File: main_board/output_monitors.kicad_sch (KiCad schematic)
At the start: 52 parts, among them U14 TL072CDR, U17 TL072CDR, U18 TL072CDR, U4 TL072CDR

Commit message: Upgrades board to v5. Adds Bonk Daddy.
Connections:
- net GND: now also R100.1, R69.1, R70.1, R71.1, R72.1, R97.1, R98.1, R99.1; no longer U14.3 (+), U14.5 (+), U17.3 (+), U17.5 (+), U18.3 (+), U18.5 (+), U4.3 (+), U4.5 (+)
- net Out0: now also U4.3 (+); no longer R69.1
- net Out1: now also U4.5 (+); no longer R70.1
- net Out2: now also U14.3 (+); no longer R71.1
- net Out3: now also U14.5 (+); no longer R72.1
- net Out4: now also U17.3 (+); no longer R97.1
- net Out5: now also U17.5 (+); no longer R98.1
- net Out6: now also U18.3 (+); no longer R99.1
- net Out7: now also U18.5 (+); no longer R100.1
- net at R72.2, U14.6 (-): now also D24.2 (A), D28.1 (K); no longer D24.1 (K), D28.2 (A)
- net at R100.2, U18.6 (-): now also D32.2 (A), D36.1 (K); no longer D32.1 (K), D36.2 (A)
- net at D29.2 (A), D33.1 (K): now also R97.2, U17.2 (-); no longer U17.1
- net at D29.1 (K), D33.2 (A): now also U17.1; no longer R97.2, U17.2 (-)
- net at R69.2, U4.2 (-): now also D21.2 (A), D25.1 (K); no longer D21.1 (K), D25.2 (A)
- net at D23.2 (A), D27.1 (K): now also R71.2, U14.2 (-); no longer U14.1
- net at D23.1 (K), D27.2 (A): now also U14.1; no longer R71.2, U14.2 (-)
- net at D31.1 (K), D35.2 (A): now also U18.1; no longer R99.2, U18.2 (-)
- net at D31.2 (A), D35.1 (K): now also R99.2, U18.2 (-); no longer U18.1
- net at D30.2 (A), D34.1 (K): now also R98.2, U17.6 (-); no longer U17.7
- net at D30.1 (K), D34.2 (A): now also U17.7; no longer R98.2, U17.6 (-)
- net at D22.2 (A), D26.1 (K): now also R70.2, U4.6 (-); no longer U4.7
- net at D22.1 (K), D26.2 (A): now also U4.7; no longer R70.2, U4.6 (-)
- new net: D24.1 (K), D28.2 (A), U14.7
- new net: D32.1 (K), D36.2 (A), U18.7
- new net: D21.1 (K), D25.2 (A), U4.1
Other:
- moved on the sheet: D21, D22, D23, D24, D25, D26, D27, D28, D29, D30, D31, D32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

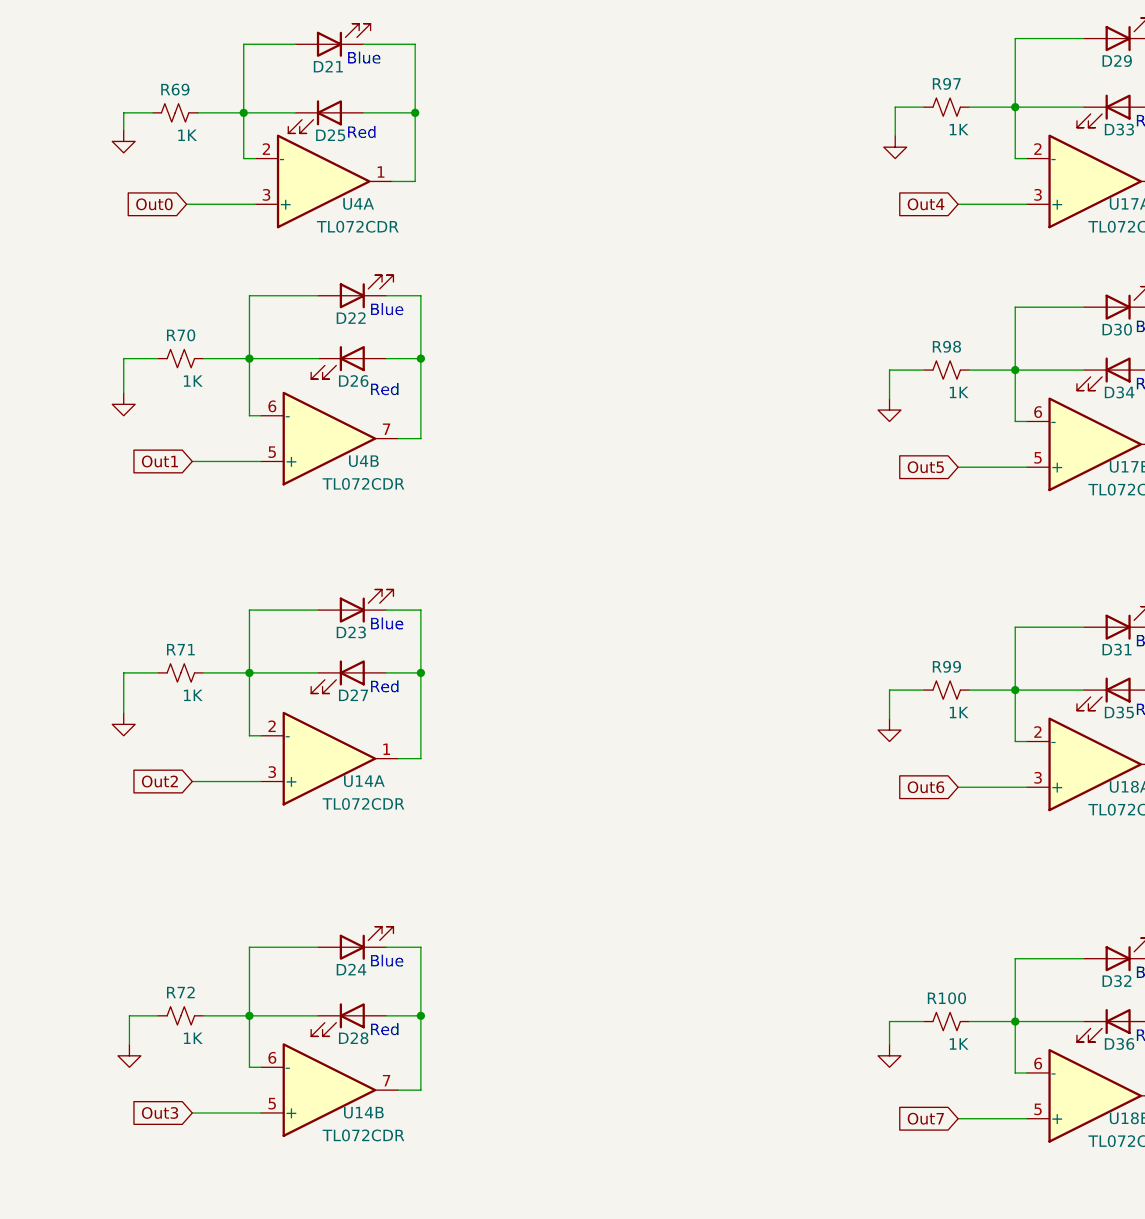
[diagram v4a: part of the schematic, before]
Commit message: LED current resistors now 2,.2K
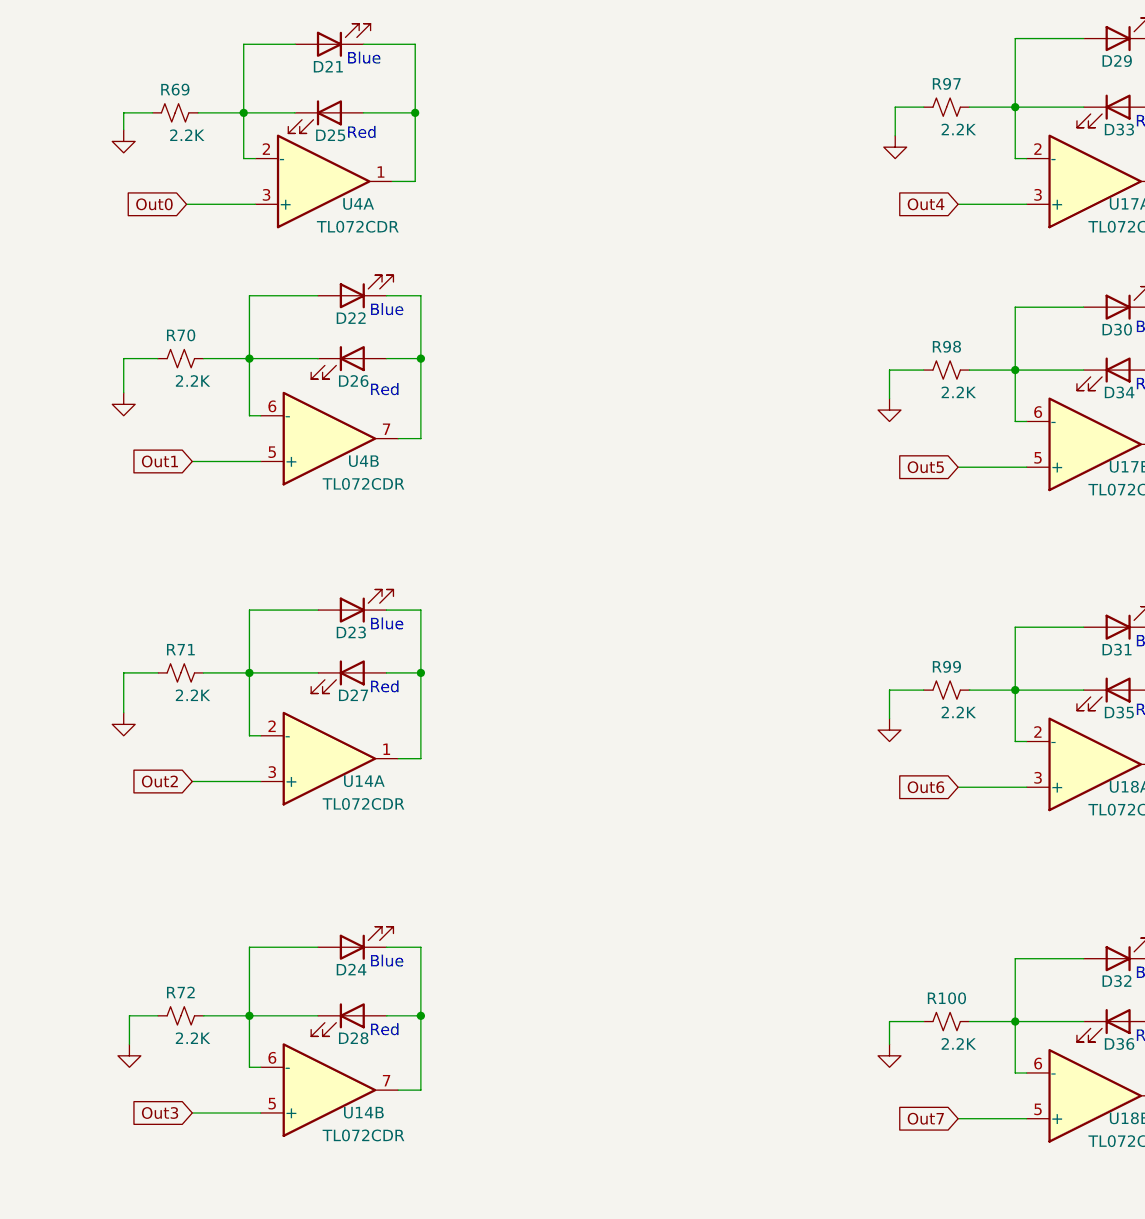
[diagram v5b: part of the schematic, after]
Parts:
- R100, R69, R70, R71, R72, R97, R98, R99: value 1K -> 2.2K;  LCSC Part # C17513 -> C17520
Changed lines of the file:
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@@
     (in_bom yes) (on_board yes)
     (property "Reference" "R72" (id 0) (at 79.375 125.095 90))
-    (property "Value" "1K" (id 1) (at 80.645 130.175 90))
+    (property "Value" "2.2K" (id 1) (at 80.645 130.175 90))
     (property "Footprint" "Resistor_SMD:R_0805_2012Metric_Pad1.20x1.40mm_HandSolder" (id 2) (at 79.375 127.635 0)
       (effects (font (size 1.27 1.27)) hide)
@@
       (effects (font (size 1.27 1.27)) hide)
     )
-    (property " LCSC Part #" "C17513" (id 5) (at 79.375 127.635 0)
+    (property " LCSC Part #" "C17520" (id 5) (at 79.375 127.635 0)
       (effects (font (size 1.27 1.27)) hide)
     )
@@
     (in_bom yes) (on_board yes)
     (property "Reference" "R100" (id 0) (at 164.465 125.73 90))
-    (property "Value" "1K" (id 1) (at 165.735 130.81 90))
+    (property "Value" "2.2K" (id 1) (at 165.735 130.81 90))
     (property "Footprint" "Resistor_SMD:R_0805_2012Metric_Pad1.20x1.40mm_HandSolder" (id 2) (at 164.465 128.27 0)
       (effects (font (size 1.27 1.27)) hide)
@@
       (effects (font (size 1.27 1.27)) hide)
     )
-    (property " LCSC Part #" "C17513" (id 5) (at 164.465 128.27 0)
+    (property " LCSC Part #" "C17520" (id 5) (at 164.465 128.27 0)
       (effects (font (size 1.27 1.27)) hide)
     )
@@
     (in_bom yes) (on_board yes)
     (property "Reference" "R69" (id 0) (at 78.74 24.765 90))
-    (property "Value" "1K" (id 1) (at 80.01 29.845 90))
+    (property "Value" "2.2K" (id 1) (at 80.01 29.845 90))
     (property "Footprint" "Resistor_SMD:R_0805_2012Metric_Pad1.20x1.40mm_HandSolder" (id 2) (at 78.74 27.305 0)
       (effects (font (size 1.27 1.27)) hide)
@@
       (effects (font (size 1.27 1.27)) hide)
     )
-    (property " LCSC Part #" "C17513" (id 5) (at 78.74 27.305 0)
+    (property " LCSC Part #" "C17520" (id 5) (at 78.74 27.305 0)
       (effects (font (size 1.27 1.27)) hide)
     )
@@
     (in_bom yes) (on_board yes)
     (property "Reference" "R99" (id 0) (at 164.465 88.9 90))
-    (property "Value" "1K" (id 1) (at 165.735 93.98 90))
+    (property "Value" "2.2K" (id 1) (at 165.735 93.98 90))
     (property "Footprint" "Resistor_SMD:R_0805_2012Metric_Pad1.20x1.40mm_HandSolder" (id 2) (at 164.465 91.44 0)
       (effects (font (size 1.27 1.27)) hide)
@@
       (effects (font (size 1.27 1.27)) hide)
     )
-    (property " LCSC Part #" "C17513" (id 5) (at 164.465 91.44 0)
+    (property " LCSC Part #" "C17520" (id 5) (at 164.465 91.44 0)
       (effects (font (size 1.27 1.27)) hide)
     )
@@
     (in_bom yes) (on_board yes)
     (property "Reference" "R98" (id 0) (at 164.465 53.34 90))
-    (property "Value" "1K" (id 1) (at 165.735 58.42 90))
+    (property "Value" "2.2K" (id 1) (at 165.735 58.42 90))
     (property "Footprint" "Resistor_SMD:R_0805_2012Metric_Pad1.20x1.40mm_HandSolder" (id 2) (at 164.465 55.88 0)
       (effects (font (size 1.27 1.27)) hide)
@@
       (effects (font (size 1.27 1.27)) hide)
     )
-    (property " LCSC Part #" "C17513" (id 5) (at 164.465 55.88 0)
+    (property " LCSC Part #" "C17520" (id 5) (at 164.465 55.88 0)
       (effects (font (size 1.27 1.27)) hide)
     )
@@
     (in_bom yes) (on_board yes)
     (property "Reference" "R70" (id 0) (at 79.375 52.07 90))
-    (property "Value" "1K" (id 1) (at 80.645 57.15 90))
+    (property "Value" "2.2K" (id 1) (at 80.645 57.15 90))
     (property "Footprint" "Resistor_SMD:R_0805_2012Metric_Pad1.20x1.40mm_HandSolder" (id 2) (at 79.375 54.61 0)
       (effects (font (size 1.27 1.27)) hide)
@@
       (effects (font (size 1.27 1.27)) hide)
     )
-    (property " LCSC Part #" "C17513" (id 5) (at 79.375 54.61 0)
+    (property " LCSC Part #" "C17520" (id 5) (at 79.375 54.61 0)
       (effects (font (size 1.27 1.27)) hide)
     )
@@
     (in_bom yes) (on_board yes)
     (property "Reference" "R71" (id 0) (at 79.375 86.995 90))
-    (property "Value" "1K" (id 1) (at 80.645 92.075 90))
+    (property "Value" "2.2K" (id 1) (at 80.645 92.075 90))
     (property "Footprint" "Resistor_SMD:R_0805_2012Metric_Pad1.20x1.40mm_HandSolder" (id 2) (at 79.375 89.535 0)
       (effects (font (size 1.27 1.27)) hide)
@@
       (effects (font (size 1.27 1.27)) hide)
     )
-    (property " LCSC Part #" "C17513" (id 5) (at 79.375 89.535 0)
+    (property " LCSC Part #" "C17520" (id 5) (at 79.375 89.535 0)
       (effects (font (size 1.27 1.27)) hide)
     )
@@
     (in_bom yes) (on_board yes)
     (property "Reference" "R97" (id 0) (at 164.465 24.13 90))
-    (property "Value" "1K" (id 1) (at 165.735 29.21 90))
+    (property "Value" "2.2K" (id 1) (at 165.735 29.21 90))
     (property "Footprint" "Resistor_SMD:R_0805_2012Metric_Pad1.20x1.40mm_HandSolder" (id 2) (at 164.465 26.67 0)
       (effects (font (size 1.27 1.27)) hide)
@@
       (effects (font (size 1.27 1.27)) hide)
     )
-    (property " LCSC Part #" "C17513" (id 5) (at 164.465 26.67 0)
-      (effects (font (size 1.27 1.27)) hide)
-    )
+    (property " LCSC Part #" "C17520" (id 5) (at 164.465 26.67 0)
+      (effects (font (size 1.27 1.27)) hide)
+    )

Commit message: Updates main_board, uses generate_boms.bat
Updates reverse protection circuitry on main board.
Updates 3.3V reference circuitry.
Uses generate_boms and retires .xlsx BOM files.
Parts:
- C35, C36, C37, C38, C39, C40, C41, C42:  LCSC Part # C49678 -> (none); LCSC Part # (none) -> C49678
- R100, R69, R70, R71, R72, R97, R98, R99:  LCSC Part # C17520 -> (none); LCSC Part # (none) -> C17520
- U14, U17, U18, U4:  LCSC Part # C6961 -> (none); LCSC Part # (none) -> C6961
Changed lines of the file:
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@@
       (effects (font (size 1.27 1.27)) hide)
     )
-    (property " LCSC Part #" "C6961" (id 5) (at 57.15 172.72 0)
+    (property "LCSC Part #" "C6961" (id 5) (at 57.15 172.72 0)
       (effects (font (size 1.27 1.27)) hide)
     )
@@
       (effects (font (size 1.27 1.27)) hide)
     )
-    (property " LCSC Part #" "C17520" (id 5) (at 79.375 127.635 0)
+    (property "LCSC Part #" "C17520" (id 5) (at 79.375 127.635 0)
       (effects (font (size 1.27 1.27)) hide)
     )
@@
       (effects (font (size 1.27 1.27)) hide)
     )
-    (property " LCSC Part #" "C6961" (id 5) (at 180.975 136.525 0)
+    (property "LCSC Part #" "C6961" (id 5) (at 180.975 136.525 0)
       (effects (font (size 1.27 1.27)) hide)
     )
@@
       (effects (font (size 1.27 1.27)) hide)
     )
-    (property " LCSC Part #" "C6961" (id 5) (at 180.975 34.925 0)
+    (property "LCSC Part #" "C6961" (id 5) (at 180.975 34.925 0)
       (effects (font (size 1.27 1.27)) hide)
     )
@@
       (effects (font (size 1.27 1.27)) hide)
     )
-    (property " LCSC Part #" "C17520" (id 5) (at 164.465 128.27 0)
+    (property "LCSC Part #" "C17520" (id 5) (at 164.465 128.27 0)
       (effects (font (size 1.27 1.27)) hide)
     )
@@
       (effects (font (size 1.27 1.27)) hide)
     )
-    (property " LCSC Part #" "C17520" (id 5) (at 78.74 27.305 0)
+    (property "LCSC Part #" "C17520" (id 5) (at 78.74 27.305 0)
       (effects (font (size 1.27 1.27)) hide)
     )
@@
       (effects (font (size 1.27 1.27)) hide)
     )
-    (property " LCSC Part #" "C17520" (id 5) (at 164.465 91.44 0)
+    (property "LCSC Part #" "C17520" (id 5) (at 164.465 91.44 0)
       (effects (font (size 1.27 1.27)) hide)
     )
@@
       (effects (font (size 1.27 1.27)) hide)
     )
-    (property " LCSC Part #" "C49678" (id 5) (at 150.495 179.705 0)
+    (property "LCSC Part #" "C49678" (id 5) (at 150.495 179.705 0)
       (effects (font (size 1.27 1.27)) hide)
     )
@@
       (effects (font (size 1.27 1.27)) hide)
     )
-    (property " LCSC Part #" "C17520" (id 5) (at 164.465 55.88 0)
+    (property "LCSC Part #" "C17520" (id 5) (at 164.465 55.88 0)
       (effects (font (size 1.27 1.27)) hide)
     )
@@
       (effects (font (size 1.27 1.27)) hide)
     )
-    (property " LCSC Part #" "C17520" (id 5) (at 79.375 54.61 0)
+    (property "LCSC Part #" "C17520" (id 5) (at 79.375 54.61 0)
       (effects (font (size 1.27 1.27)) hide)
     )
@@
       (effects (font (size 1.27 1.27)) hide)
     )
-    (property " LCSC Part #" "C6961" (id 5) (at 36.83 172.72 0)
+    (property "LCSC Part #" "C6961" (id 5) (at 36.83 172.72 0)
       (effects (font (size 1.27 1.27)) hide)
     )
@@
       (effects (font (size 1.27 1.27)) hide)
     )
-    (property " LCSC Part #" "C6961" (id 5) (at 95.885 63.5 0)
+    (property "LCSC Part #" "C6961" (id 5) (at 95.885 63.5 0)
       (effects (font (size 1.27 1.27)) hide)
     )
@@
       (effects (font (size 1.27 1.27)) hide)
     )
-    (property " LCSC Part #" "C6961" (id 5) (at 180.975 99.695 0)
+    (property "LCSC Part #" "C6961" (id 5) (at 180.975 99.695 0)
       (effects (font (size 1.27 1.27)) hide)
     )
@@
       (effects (font (size 1.27 1.27)) hide)
     )
-    (property " LCSC Part #" "C17520" (id 5) (at 79.375 89.535 0)
+    (property "LCSC Part #" "C17520" (id 5) (at 79.375 89.535 0)
       (effects (font (size 1.27 1.27)) hide)
     )
@@
       (effects (font (size 1.27 1.27)) hide)
     )
-    (property " LCSC Part #" "C6961" (id 5) (at 95.885 99.06 0)
+    (property "LCSC Part #" "C6961" (id 5) (at 95.885 99.06 0)
       (effects (font (size 1.27 1.27)) hide)
     )
@@
       (effects (font (size 1.27 1.27)) hide)
     )
-    (property " LCSC Part #" "C49678" (id 5) (at 142.875 179.705 0)
+    (property "LCSC Part #" "C49678" (id 5) (at 142.875 179.705 0)
       (effects (font (size 1.27 1.27)) hide)
     )
@@
       (effects (font (size 1.27 1.27)) hide)
     )
-    (property " LCSC Part #" "C6961" (id 5) (at 46.99 172.72 0)
+    (property "LCSC Part #" "C6961" (id 5) (at 46.99 172.72 0)
       (effects (font (size 1.27 1.27)) hide)
     )
@@
       (effects (font (size 1.27 1.27)) hide)
     )
-    (property " LCSC Part #" "C17520" (id 5) (at 164.465 26.67 0)
+    (property "LCSC Part #" "C17520" (id 5) (at 164.465 26.67 0)
       (effects (font (size 1.27 1.27)) hide)
     )
@@
       (effects (font (size 1.27 1.27)) hide)
     )
-    (property " LCSC Part #" "C49678" (id 5) (at 135.255 168.275 0)
+    (property "LCSC Part #" "C49678" (id 5) (at 135.255 168.275 0)
       (effects (font (size 1.27 1.27)) hide)
     )
@@
       (effects (font (size 1.27 1.27)) hide)
     )
-    (property " LCSC Part #" "C49678" (id 5) (at 135.255 179.705 0)
+    (property "LCSC Part #" "C49678" (id 5) (at 135.255 179.705 0)
       (effects (font (size 1.27 1.27)) hide)
     )
@@
       (effects (font (size 1.27 1.27)) hide)
     )
-    (property " LCSC Part #" "C49678" (id 5) (at 150.495 168.275 0)
+    (property "LCSC Part #" "C49678" (id 5) (at 150.495 168.275 0)
       (effects (font (size 1.27 1.27)) hide)
     )
@@
       (effects (font (size 1.27 1.27)) hide)
     )
-    (property " LCSC Part #" "C49678" (id 5) (at 127.635 168.275 0)
+    (property "LCSC Part #" "C49678" (id 5) (at 127.635 168.275 0)
       (effects (font (size 1.27 1.27)) hide)
     )
@@
       (effects (font (size 1.27 1.27)) hide)
     )
-    (property " LCSC Part #" "C6961" (id 5) (at 95.25 34.925 0)
+    (property "LCSC Part #" "C6961" (id 5) (at 95.25 34.925 0)
       (effects (font (size 1.27 1.27)) hide)
     )
@@
       (effects (font (size 1.27 1.27)) hide)
     )
-    (property " LCSC Part #" "C49678" (id 5) (at 142.875 168.275 0)
+    (property "LCSC Part #" "C49678" (id 5) (at 142.875 168.275 0)
       (effects (font (size 1.27 1.27)) hide)
     )
@@
       (effects (font (size 1.27 1.27)) hide)
     )
-    (property " LCSC Part #" "C6961" (id 5) (at 180.975 64.135 0)
+    (property "LCSC Part #" "C6961" (id 5) (at 180.975 64.135 0)
       (effects (font (size 1.27 1.27)) hide)
     )
@@
       (effects (font (size 1.27 1.27)) hide)
     )
-    (property " LCSC Part #" "C49678" (id 5) (at 127.635 179.705 0)
+    (property "LCSC Part #" "C49678" (id 5) (at 127.635 179.705 0)
       (effects (font (size 1.27 1.27)) hide)
     )
@@
       (effects (font (size 1.27 1.27)) hide)
     )
-    (property " LCSC Part #" "C6961" (id 5) (at 67.31 172.72 0)
+    (property "LCSC Part #" "C6961" (id 5) (at 67.31 172.72 0)
       (effects (font (size 1.27 1.27)) hide)
     )
@@
       (effects (font (size 1.27 1.27)) hide)
     )
-    (property " LCSC Part #" "C6961" (id 5) (at 95.885 135.89 0)
-      (effects (font (size 1.27 1.27)) hide)
-    )
+    (property "LCSC Part #" "C6961" (id 5) (at 95.885 135.89 0)
+      (effects (font (size 1.27 1.27)) hide)
+    )
